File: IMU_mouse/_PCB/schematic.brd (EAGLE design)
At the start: 160 x 100 mm, 43 parts, among them IC1 REG1117, M1 WIRELESS-NRF24L01, U1 GY-521MPU6050

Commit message: IMU mouse PCB update
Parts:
- removed C2, C3, NRF: (no value), rcl:E2,5-5
- removed C5, C7, NRF_2: (no value), rcl:C0805
- removed D1: (no value), SparkFun-LED:LED_3MM
- removed J1, J3, J4, NRF_POW1: (no value), SparkFun-Connectors:1X02_LOCK
- removed JP2, JP3, JP4, JP5, NRF_POW: JUMPER-SMT_2_NO_SILK, SparkFun-Jumpers:SMT-JUMPER_2_NO_SILK
- removed M1: WIRELESS-NRF24L01, diy-modules:WIRELESS-NRF24L01
- removed R2, R3, R4, R5: (no value), rcl:R0805
- added JP_L, JP_R: (no value), SparkFun-Jumpers:SMT-JUMPER_2_NC_TRACE_SILK
- LEFT, RIGHT: value MOMENTARY-SWITCH-SPST-PTH-6.0MM -> (none)
- moved H2 224.1 mm to (82.3, 32.4)
- moved H4 218.8 mm to (82.3, 4.06)
- moved C_5V 214.9 mm to (29.8, 32.1)
- moved C_5V_1 214.9 mm to (29.8, 25.7)
- moved MICRO_2 212.5 mm to (70.8, 30.5)
- moved J6 209.1 mm to (64.1, 27.2), turned to 180 degrees
- moved SHIELD 207.8 mm to (57.3, 30.7)
- moved JP_SDA 203.3 mm to (21.6, 30.4)
- moved JP_SCL 198.2 mm to (25.0, 30.4)
- moved OUT_2 195.8 mm to (51.9, 34.3), turned to 180 degrees
- moved OUT 193.7 mm to (52.1, 30.4), turned to 90 degrees
- moved GY-521 191.8 mm to (9.40, 26.2)
- moved IN_2 188.6 mm to (45.8, 34.2)
- moved IN 186.9 mm to (45.9, 30.4), turned to 270 degrees
- moved IC1 178.7 mm to (37.6, 30.9), turned to 90 degrees
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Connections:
- removed net N$5: B1.9, M1.4
- removed net N$6: M1.2, NRF_POW.2, NRF_POW1.2
- net 3.3V: no longer NRF.+, NRF_2.1, NRF_POW.1, NRF_POW1.1
- net 5V: now also LEFT.3, RIGHT.3; no longer LEFT.1, RIGHT.1
- net GND: no longer M1.1, NRF.-, NRF_2.2
- net N$1: now also J2.2, JP_L.2, LEFT.1; no longer B1.15, M1.7
- net N$2: now also J2.1, JP_R.2, RIGHT.1; no longer B1.14, M1.6
- net N$3: now also B1.8, JP_R.1; no longer B1.16, M1.5
- net N$4: now also B1.9, JP_L.1; no longer B1.10, M1.3
- net N$8: now also JP_SDA.2; no longer JP_SDA.1
- net N$9: now also JP_SCL.2; no longer JP_SCL.1
- net SCL: now also JP_SCL.1; no longer JP_SCL.2
- net SDA: now also JP_SDA.1; no longer JP_SDA.2
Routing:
- net 5V: track 0.00 -> 106.7 mm
- net GND: track 0.00 -> 96.6 mm, vias 0 -> 1
- net N$8: track 0.00 -> 48.1 mm, vias 0 -> 1
- net N$9: track 0.00 -> 47.2 mm, vias 0 -> 2
- net N$3: track 0.00 -> 41.5 mm
- net N$4: track 0.00 -> 37.3 mm, vias 0 -> 1
- net N$1: track 0.00 -> 34.2 mm
- net N$2: track 0.00 -> 31.6 mm
- net N$7: track 0.00 -> 21.8 mm
- net 3.3V: track 0.00 -> 19.8 mm, vias 0 -> 1
- net SCL: track 0.00 -> 9.64 mm
- net SDA: track 0.00 -> 9.32 mm
- net D+: track 0.00 -> 8.11 mm
- net D-: track 0.00 -> 4.94 mm
- net N$12: track 0.00 -> 4.45 mm
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- added copper zone on layer 1, net GND
- added copper zone on layer 16, net GND
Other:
- board size 160 x 100 mm -> 86.3 x 36.5 mm
- board text added: "d+"
- board text added: "d-"

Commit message: IMU mouse PCB
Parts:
- moved RIGHT 0.05 mm to (12.5, 4.27)
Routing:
- net GND: track 96.6 -> 0.00 mm, vias 1 -> 0
- net N$4: track 37.3 -> 63.8 mm
- net N$3: track 41.5 -> 60.2 mm
- net N$8: track 48.1 -> 44.7 mm, vias 1 -> 3
- net N$9: track 47.2 -> 45.2 mm, vias 2 -> 3
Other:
- outline, holes or cut-outs redrawn

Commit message: update
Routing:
- net GND: track 0.00 -> 4.11 mm, vias 0 -> 4
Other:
- board size 86.3 x 36.5 mm -> 86.4 x 36.5 mm
- board text added: "CUTOUT"
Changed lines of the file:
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@@
 <text x="62.23" y="25.654" size="1.1176" layer="21" font="vector" rot="R180">d+</text>
 <text x="64.77" y="25.654" size="1.1176" layer="21" font="vector" rot="R180">d-</text>
-<wire x1="82.2706" y1="36.4998" x2="83.947" y2="36.4998" width="0.0508" layer="20"/>
-<wire x1="83.947" y1="36.4998" x2="86.3346" y2="34.1122" width="0.0508" layer="20"/>
-<wire x1="86.3346" y1="34.1122" x2="86.3346" y2="2.3622" width="0.0508" layer="20"/>
-<wire x1="86.3346" y1="2.3622" x2="83.9724" y2="0" width="0.0508" layer="20"/>
-<wire x1="83.9724" y1="0" x2="2.4384" y2="0" width="0.0508" layer="20"/>
-<wire x1="2.4384" y1="0" x2="0" y2="2.4384" width="0.0508" layer="20"/>
-<wire x1="0" y1="2.4384" x2="0" y2="34.1376" width="0.0508" layer="20"/>
-<wire x1="0" y1="34.1376" x2="2.3622" y2="36.4998" width="0.0508" layer="20"/>
-<wire x1="2.3622" y1="36.4998" x2="82.2706" y2="36.4998" width="0.0508" layer="20"/>
+<text x="57.8104" y="13.2334" size="1.778" layer="21" font="vector">CUTOUT</text>
+<wire x1="4.0386" y1="36.4998" x2="2.3368" y2="36.4998" width="0.0254" layer="20"/>
+<wire x1="2.3368" y1="36.4998" x2="0" y2="34.163" width="0.0254" layer="20"/>
+<wire x1="0" y1="34.163" x2="-0.0254" y2="34.1376" width="0.0254" layer="20"/>
+<wire x1="-0.0254" y1="34.1376" x2="-0.0254" y2="32.4358" width="0.0254" layer="20"/>
+<wire x1="-0.0254" y1="32.4358" x2="-0.0254" y2="2.4384" width="0.0254" layer="20"/>
+<wire x1="-0.0254" y1="2.4384" x2="2.3622" y2="0.0508" width="0.0254" layer="20"/>
+<wire x1="2.3622" y1="0.0508" x2="2.413" y2="0" width="0.0254" layer="20"/>
+<wire x1="2.413" y1="0" x2="4.2418" y2="0" width="0.0254" layer="20"/>
+<wire x1="4.2418" y1="0" x2="83.9978" y2="0" width="0.0254" layer="20"/>
+<wire x1="83.9978" y1="0" x2="86.233" y2="2.2352" width="0.0254" layer="20"/>
+<wire x1="86.233" y1="2.2352" x2="86.3854" y2="2.3876" width="0.0254" layer="20"/>
+<wire x1="86.3854" y1="2.3876" x2="86.3854" y2="4.0386" width="0.0254" layer="20"/>
+<wire x1="86.3854" y1="4.0386" x2="86.3854" y2="8.0518" width="0.0254" layer="20"/>
+<wire x1="86.3854" y1="8.0518" x2="84.582" y2="9.8552" width="0.0254" layer="20"/>
+<wire x1="84.582" y1="9.8552" x2="79.2734" y2="9.8552" width="0.0254" layer="20"/>
+<wire x1="79.2734" y1="9.8552" x2="78.7146" y2="9.2964" width="0.0254" layer="20"/>
+<wire x1="78.7146" y1="9.2964" x2="78.486" y2="9.0678" width="0.0254" layer="20"/>
+<wire x1="78.486" y1="9.0678" x2="47.5996" y2="9.0678" width="0.0254" layer="20"/>
+<wire x1="47.5996" y1="9.0678" x2="43.688" y2="5.1562" width="0.0254" layer="20"/>
+<wire x1="43.688" y1="5.1562" x2="40.132" y2="5.1562" width="0.0254" layer="20"/>
+<wire x1="40.132" y1="5.1562" x2="38.8366" y2="6.4516" width="0.0254" layer="20"/>
+<wire x1="38.8366" y1="6.4516" x2="38.8366" y2="11.8618" width="0.0254" layer="20"/>
+<wire x1="38.8366" y1="11.8618" x2="45.4152" y2="18.4404" width="0.0254" layer="20"/>
+<wire x1="45.4152" y1="18.4404" x2="78.359" y2="18.4404" width="0.0254" layer="20"/>
+<wire x1="78.359" y1="18.4404" x2="79.9084" y2="18.4404" width="0.0254" layer="20"/>
+<wire x1="79.9084" y1="18.4404" x2="85.9536" y2="24.4856" width="0.0254" layer="20"/>
+<wire x1="85.9536" y1="24.4856" x2="86.36" y2="24.892" width="0.0254" layer="20"/>
+<wire x1="86.36" y1="24.892" x2="86.36" y2="32.4104" width="0.0254" layer="20"/>
+<wire x1="86.36" y1="32.4104" x2="86.36" y2="34.0868" width="0.0254" layer="20"/>
+<wire x1="86.36" y1="34.0868" x2="83.9216" y2="36.4998" width="0.0254" layer="20"/>
+<wire x1="83.9216" y1="36.4998" x2="4.064" y2="36.4998" width="0.0254" layer="20"/>
+<wire x1="4.064" y1="36.4998" x2="4.0386" y2="36.4998" width="0.0254" layer="20"/>
 </plain>
 <attributes>
@@
 <vertex x="89.8144" y="38.3286"/>
 </polygon>
+<via x="26.3398" y="4.8006" extent="1-16" drill="0.35"/>
+<via x="75.184" y="2.3876" extent="1-16" drill="0.35"/>
+<via x="71.0692" y="2.3876" extent="1-16" drill="0.35"/>
+<wire x1="71.0692" y1="2.3876" x2="75.184" y2="2.3876" width="0.635" layer="1"/>
+<via x="12.573" y="34.6456" extent="1-16" drill="0.35"/>
 </signal>
 <signal name="RAW">

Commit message: update
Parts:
- removed C_5V: (no value), rcl:E2,5-5
- added 3.3V: (no value), SparkFun-Connectors:1X03
- added GY521_2: (no value), SparkFun-Connectors:1X08
- added GY_3.3V: 3.3V, SparkFun-Jumpers:SMT-JUMPER_2_NO_NO-SILK
- added GY_5V_DEFAULT: 5V, SparkFun-Jumpers:SMT-JUMPER_2_NC_TRACE_SILK
- added POWER: FEMALE 2x3, SparkFun-Connectors:2X3
- added RESET1: (no value), SparkFun-Switches:TACTILE_SWITCH_PTH_6.0MM
- added RESET2: 6*3.5mm, SparkFun-Switches:TACTILE_SWITCH_SMD_6.0X3.5MM
- IN, OUT: value (none) -> 100nF
- moved SHIELD 28.1 mm to (49.2, 3.81), turned to 0 degrees
- moved C_5V_1 22.7 mm to (52.1, 29.8), turned to 270 degrees
- moved OUT 22.5 mm to (74.6, 28.7)
- moved OUT_2 22.5 mm to (74.4, 32.7)
- moved IN 22.5 mm to (68.4, 28.7)
- moved IN_2 22.5 mm to (68.3, 32.6)
- moved IC1 22.5 mm to (60.1, 29.8)
- moved MICRO_2 16.6 mm to (74.5, 14.3), flipped to the bottom, turned to 180 degrees
- moved J6 16.4 mm to (65.5, 10.9), turned to 0 degrees
- moved JP_SCL 4.00 mm to (21.8, 32.8), turned to 90 degrees
- moved JP_SDA 2.99 mm to (19.8, 32.8), turned to 90 degrees
- moved GY-521 1.40 mm to (9.40, 27.6)
- moved J2 1.09 mm to (34.4, 20.5)
- moved JP_L 0.90 mm to (39.9, 23.2)
- moved JP_R 0.90 mm to (39.9, 20.3)
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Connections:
- new net N$5: GY521_2.1, GY_3.3V.1, GY_5V_DEFAULT.1, U1.VCC
- new net N$6: B1.22, RESET1.1, RESET2.1
- net 3.3V: now also 3.3V.1, 3.3V.2, 3.3V.3, GY_3.3V.2
- net 5V: now also GY_5V_DEFAULT.2, POWER.1, POWER.3, POWER.5; no longer C_5V.+, LEFT.3, RIGHT.3, U1.VCC
- net GND: now also GY521_2.2, LEFT.3, POWER.2, POWER.4, POWER.6, RESET1.3, RESET2.2, RIGHT.3; no longer C_5V.-
- net N$10: now also GY521_2.8
- net N$11: now also GY521_2.7
- net N$12: now also GY521_2.6
- net N$13: now also GY521_2.5
- net SCL: now also GY521_2.3
- net SDA: now also GY521_2.4
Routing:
- net 3.3V: track 19.8 -> 78.8 mm, vias 1 -> 0
- net N$6: track 0.00 -> 28.7 mm
- net N$4: track 63.8 -> 36.6 mm, vias 1 -> 2
- net N$3: track 60.2 -> 33.1 mm, vias 0 -> 2
- net N$7: track 21.8 -> 40.8 mm, vias 0 -> 1
- net N$5: track 0.00 -> 18.1 mm
- net N$9: track 45.2 -> 52.9 mm, vias 3 -> 2
- net N$8: track 44.7 -> 52.4 mm, vias 3 -> 2
- net GND: track 4.11 -> 0.00 mm, vias 4 -> 13
- net D-: track 4.94 -> 8.24 mm
- net D+: track 8.11 -> 5.26 mm
- net N$13: track 4.24 -> 6.19 mm
- net N$11: track 4.26 -> 6.19 mm
- net N$10: track 4.45 -> 6.36 mm
- net N$12: track 4.45 -> 6.36 mm
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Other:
- outline, holes or cut-outs redrawn
- board text added: "3.3V"
- board text added: "5V"
- board text added: "GND"
- board text removed: "CUTOUT"

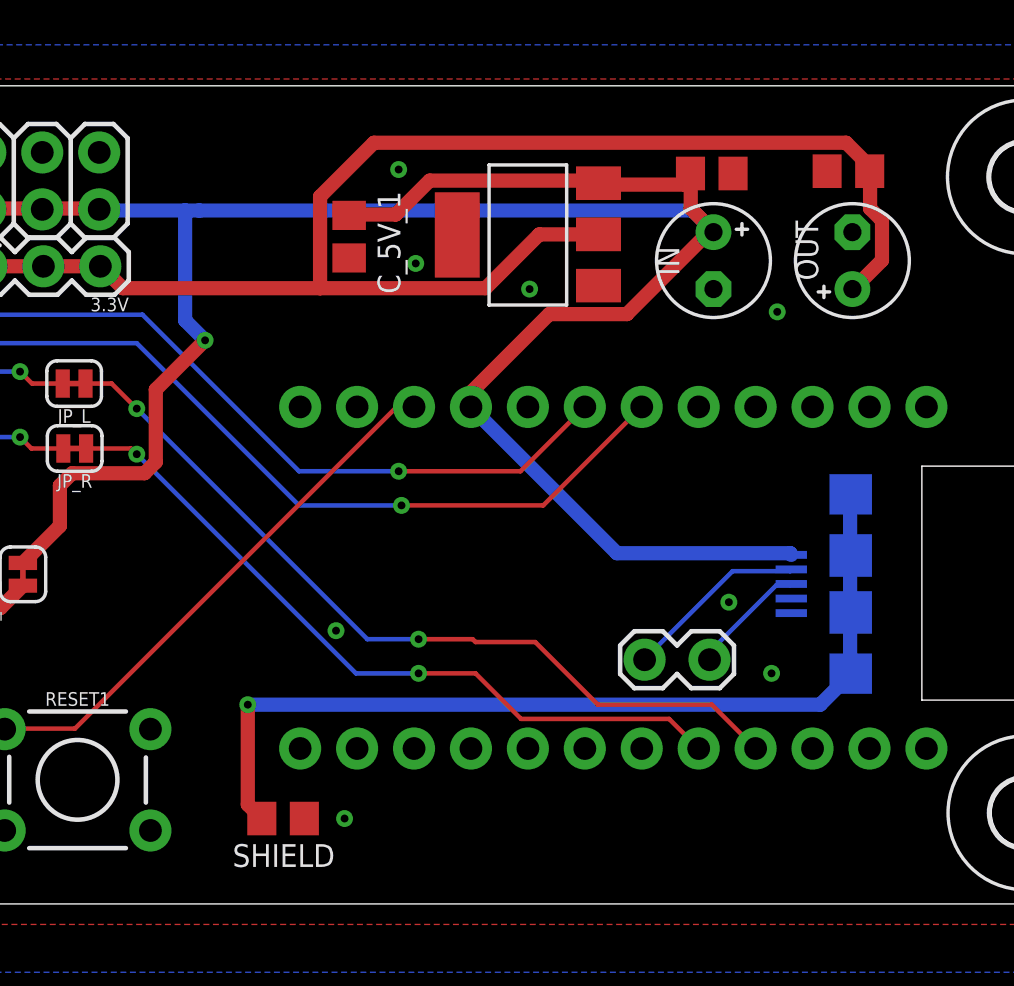
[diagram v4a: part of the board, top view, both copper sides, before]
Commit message: IMU code, PCB update
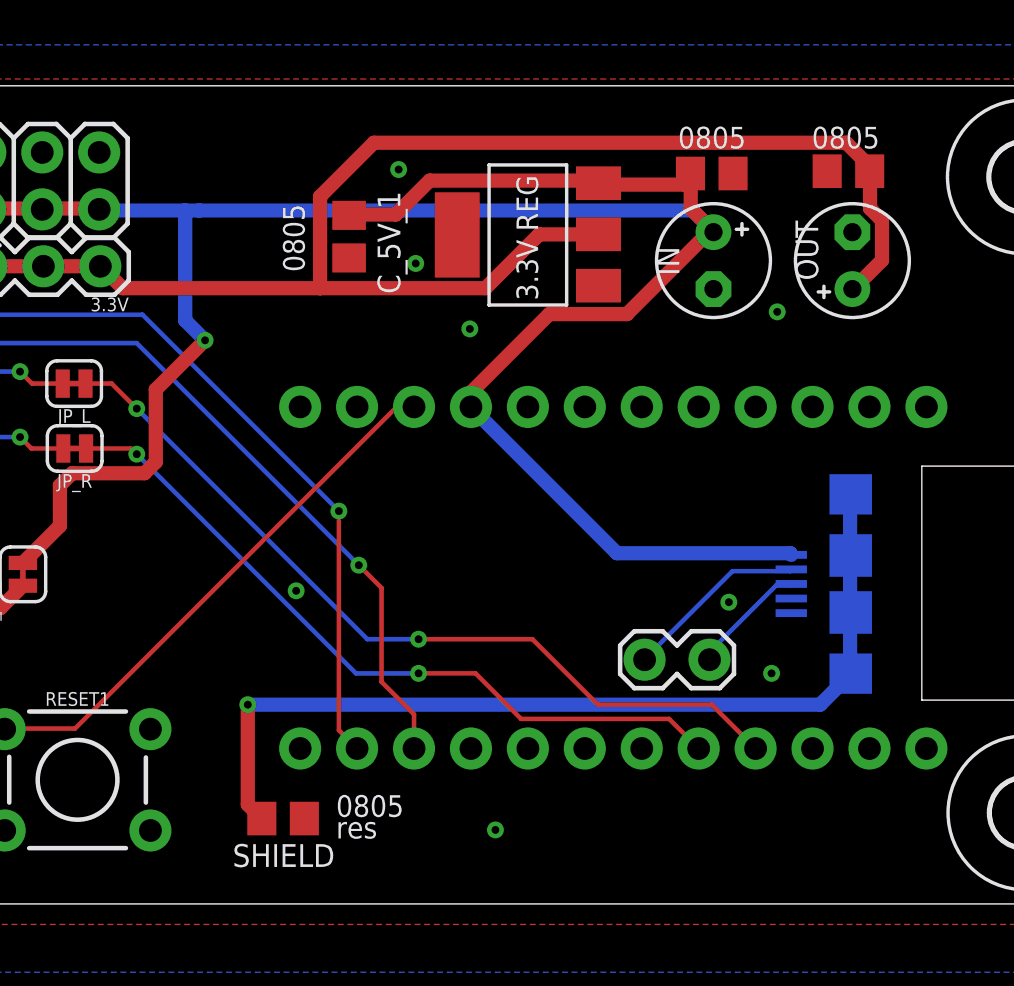
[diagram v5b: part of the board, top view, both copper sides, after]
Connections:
- net GND: no longer B1.3
- net N$8: now also B1.2; no longer B1.19
- net N$9: now also B1.3; no longer B1.18
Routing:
- net N$9: track 52.9 -> 48.8 mm
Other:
- board text added: "0805"
- board text added: "0805 res"
- board text added: "3.3V REG"
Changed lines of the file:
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@@
 <layer number="43" name="vRestrict" color="2" fill="10" visible="no" active="yes"/>
 <layer number="44" name="Drills" color="7" fill="1" visible="no" active="yes"/>
-<layer number="45" name="Holes" color="7" fill="1" visible="no" active="yes"/>
+<layer number="45" name="Holes" color="7" fill="1" visible="yes" active="yes"/>
 <layer number="46" name="Milling" color="3" fill="1" visible="no" active="yes"/>
 <layer number="47" name="Measures" color="7" fill="1" visible="no" active="yes"/>
@@
 <text x="34.163" y="31.369" size="1.0668" layer="21" font="vector" rot="R180">5V</text>
 <text x="34.29" y="28.956" size="1.0668" layer="21" font="vector" rot="R180">3.3V</text>
+<text x="51.562" y="2.921" size="0.9652" layer="21" font="vector" distance="0">0805
+res</text>
+<text x="50.165" y="28.194" size="0.9652" layer="21" font="vector" distance="0" rot="R90">0805</text>
+<text x="69.85" y="34.671" size="0.9652" layer="21" font="vector" distance="0" rot="R180">0805</text>
+<text x="75.819" y="34.671" size="0.9652" layer="21" font="vector" distance="0" rot="R180">0805</text>
+<text x="60.579" y="26.924" size="0.9652" layer="21" font="vector" distance="0" rot="R90">3.3V REG</text>
 </plain>
 <attributes>
@@
 <contactref element="B1" pad="4"/>
 <contactref element="B1" pad="23"/>
-<contactref element="B1" pad="3"/>
 <contactref element="U1" pad="GND"/>
 <contactref element="IC1" pad="1"/>
@@
 <via x="54.356" y="32.766" extent="1-16" drill="0.35"/>
 <via x="71.247" y="26.416" extent="1-16" drill="0.35"/>
-<via x="60.198" y="27.432" extent="1-16" drill="0.35"/>
-<via x="51.562" y="12.192" extent="1-16" drill="0.35"/>
+<via x="57.531" y="25.654" extent="1-16" drill="0.35"/>
+<via x="49.784" y="13.97" extent="1-16" drill="0.35"/>
 <via x="70.993" y="10.287" extent="1-16" drill="0.35"/>
 <via x="12.573" y="34.29" extent="1-16" drill="0.35"/>
@@
 <via x="15.113" y="15.494" extent="1-16" drill="0.35"/>
 <via x="22.606" y="15.24" extent="1-16" drill="0.35"/>
-<via x="51.943" y="3.81" extent="1-16" drill="0.35"/>
+<via x="58.674" y="3.302" extent="1-16" drill="0.35"/>
 </signal>
 <signal name="RAW">
@@
 </signal>
 <signal name="N$8">
-<contactref element="B1" pad="19"/>
 <contactref element="JP_SDA" pad="2"/>
 <via x="28.448" y="33.401" extent="1-16" drill="0.35"/>
@@
 <wire x1="25.019" y1="34.417" x2="26.035" y2="33.401" width="0.2032" layer="1"/>
 <wire x1="26.035" y1="33.401" x2="28.448" y2="33.401" width="0.2032" layer="1"/>
-<wire x1="59.7916" y1="19.304" x2="62.6618" y2="22.1742" width="0.2032" layer="1"/>
-<via x="54.356" y="19.304" extent="1-16" drill="0.35"/>
-<wire x1="54.356" y1="19.304" x2="59.7916" y2="19.304" width="0.2032" layer="1"/>
-<wire x1="54.356" y1="19.304" x2="49.911" y2="19.304" width="0.2032" layer="16"/>
+<via x="51.689" y="17.526" extent="1-16" drill="0.35"/>
 <wire x1="42.926" y1="26.289" x2="33.782" y2="26.289" width="0.2032" layer="16"/>
 <wire x1="33.782" y1="26.289" x2="31.115" y2="28.956" width="0.2032" layer="16"/>
@@
 <wire x1="31.115" y1="31.623" x2="29.337" y2="33.401" width="0.2032" layer="16"/>
 <wire x1="29.337" y1="33.401" x2="28.448" y2="33.401" width="0.2032" layer="16"/>
-<wire x1="49.911" y1="19.304" x2="42.926" y2="26.289" width="0.2032" layer="16"/>
+<contactref element="B1" pad="2"/>
+<wire x1="51.689" y1="17.526" x2="42.926" y2="26.289" width="0.2032" layer="16"/>
+<wire x1="51.689" y1="7.747" x2="52.5018" y2="6.9342" width="0.2032" layer="1"/>
+<wire x1="51.689" y1="17.526" x2="51.689" y2="7.747" width="0.2032" layer="1"/>
 </signal>
 <signal name="N$9">
-<contactref element="B1" pad="18"/>
 <contactref element="JP_SCL" pad="2"/>
 <via x="28.448" y="32.004" extent="1-16" drill="0.35"/>
@@
 <wire x1="25.527" y1="32.004" x2="28.448" y2="32.004" width="0.2032" layer="1"/>
 <wire x1="24.1808" y1="33.3502" x2="25.527" y2="32.004" width="0.2032" layer="1"/>
-<wire x1="60.8076" y1="17.78" x2="65.2018" y2="22.1742" width="0.2032" layer="1"/>
-<via x="54.483" y="17.78" extent="1-16" drill="0.35"/>
-<wire x1="54.483" y1="17.78" x2="60.8076" y2="17.78" width="0.2032" layer="1"/>
-<wire x1="54.483" y1="17.78" x2="49.911" y2="17.78" width="0.2032" layer="16"/>
-<wire x1="49.911" y1="17.78" x2="42.672" y2="25.019" width="0.2032" layer="16"/>
+<via x="52.578" y="15.113" extent="1-16" drill="0.35"/>
 <wire x1="42.672" y1="25.019" x2="33.274" y2="25.019" width="0.2032" layer="16"/>
 <wire x1="28.448" y1="29.845" x2="28.448" y2="32.004" width="0.2032" layer="16"/>
 <wire x1="33.274" y1="25.019" x2="28.448" y2="29.845" width="0.2032" layer="16"/>
+<contactref element="B1" pad="3"/>
+<wire x1="52.578" y1="15.113" x2="42.672" y2="25.019" width="0.2032" layer="16"/>
+<wire x1="52.578" y1="15.113" x2="53.594" y2="14.097" width="0.2032" layer="1"/>
+<wire x1="53.594" y1="14.097" x2="53.594" y2="9.906" width="0.2032" layer="1"/>
+<wire x1="53.594" y1="9.906" x2="55.0418" y2="8.4582" width="0.2032" layer="1"/>
+<wire x1="55.0418" y1="8.4582" x2="55.0418" y2="6.9342" width="0.2032" layer="1"/>
 </signal>
 <signal name="N$11">
@@
 <wire x1="70.2818" y1="6.9342" x2="68.326" y2="8.89" width="0.2032" layer="1"/>
 <wire x1="68.326" y1="8.89" x2="63.246" y2="8.89" width="0.2032" layer="1"/>
-<wire x1="63.246" y1="8.89" x2="60.452" y2="11.684" width="0.2032" layer="1"/>
-<wire x1="57.785" y1="11.684" x2="60.452" y2="11.684" width="0.2032" layer="1"/>
 <via x="55.245" y="11.811" extent="1-16" drill="0.35"/>
-<wire x1="55.245" y1="11.811" x2="57.658" y2="11.811" width="0.2032" layer="1"/>
-<wire x1="57.658" y1="11.811" x2="57.785" y2="11.684" width="0.2032" layer="1"/>
 <via x="42.672" y="22.098" extent="1-16" drill="0.35"/>
 <wire x1="40.386" y1="23.2156" x2="41.5544" y2="23.2156" width="0.2032" layer="1"/>
@@
 <wire x1="42.672" y1="22.098" x2="52.959" y2="11.811" width="0.2032" layer="16"/>
 <wire x1="52.959" y1="11.811" x2="55.245" y2="11.811" width="0.2032" layer="16"/>
+<wire x1="60.325" y1="11.811" x2="55.245" y2="11.811" width="0.2032" layer="1"/>
+<wire x1="63.246" y1="8.89" x2="60.325" y2="11.811" width="0.2032" layer="1"/>
 </signal>
 <signal name="N$5" class="1">
@@
 </drawing>
 <compatibility>
+<note version="6.3" minversion="6.2.2" severity="warning">
+Since Version 6.2.2 text objects can contain more than one line,
+which will not be processed correctly with this version.
+</note>
 <note version="8.2" severity="warning">
 Since Version 8.2, EAGLE supports online libraries. The ids

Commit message: IMU mouse update
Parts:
- B1: value SPARKFUN_PRO_MICRO -> ARDUINO_PRO_MICRO
